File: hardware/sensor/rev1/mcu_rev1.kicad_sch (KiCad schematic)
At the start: 20 parts, among them IC1 STM8L051F3P6, J1 G8250041000YEU, J2 M20-9770342

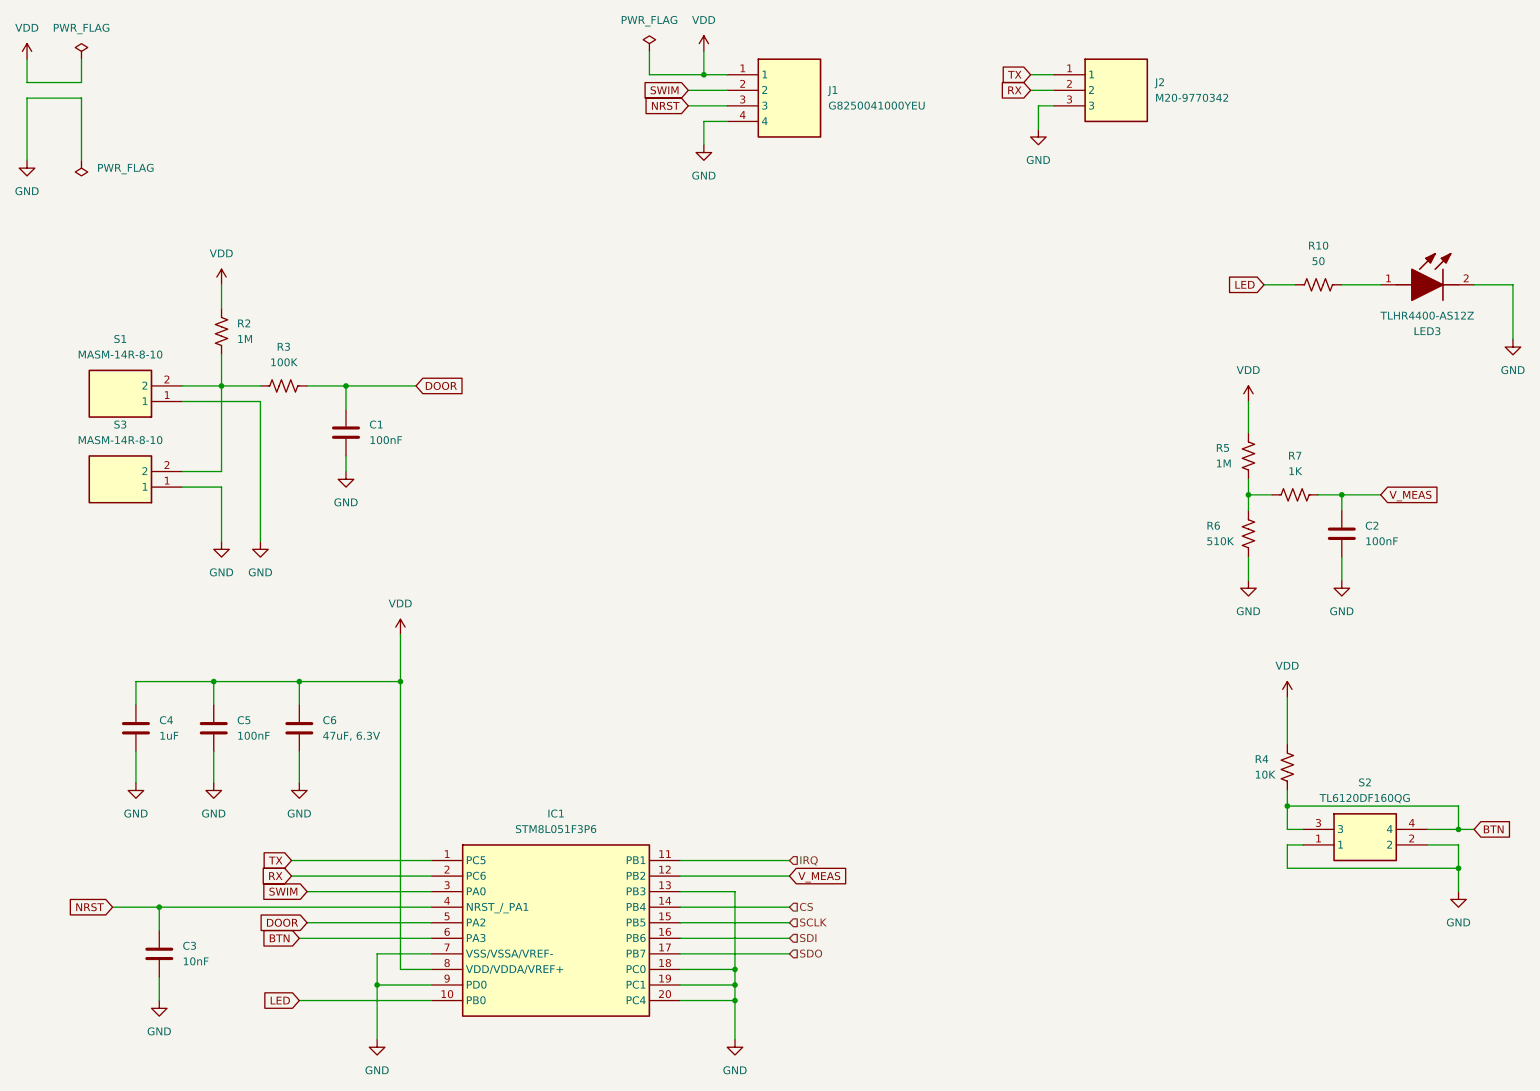
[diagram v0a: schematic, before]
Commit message: EG-49 Several components addes, such as bulk capacitors, battery holder, MCU and reed switches.
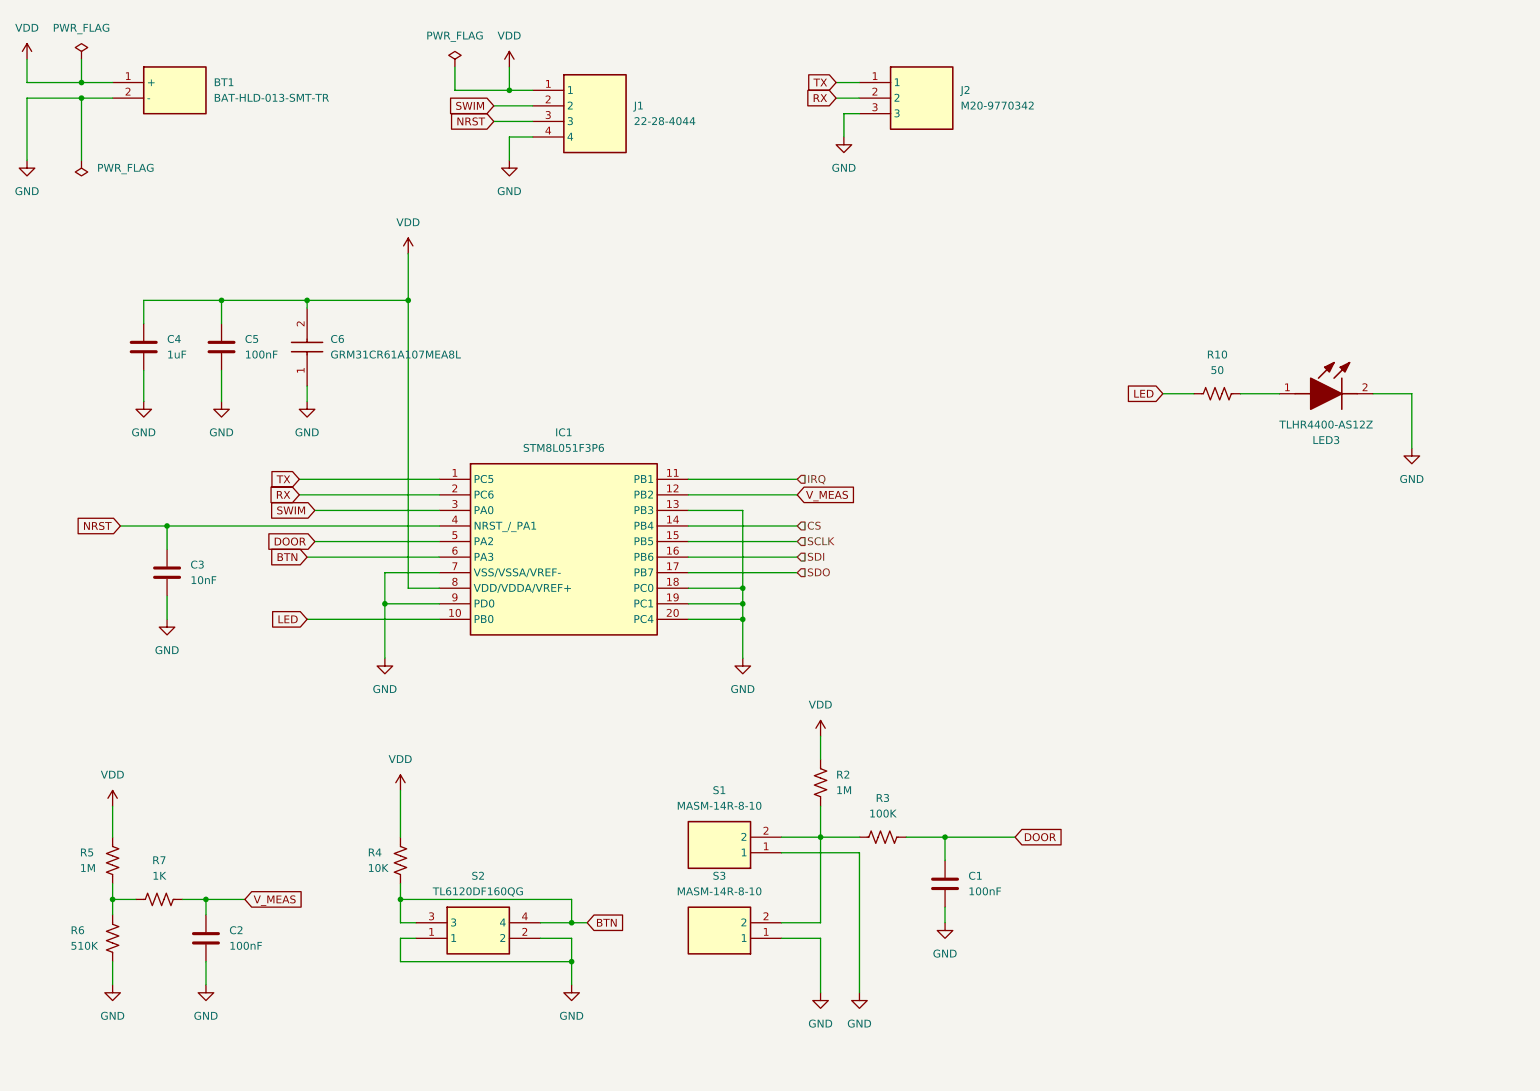
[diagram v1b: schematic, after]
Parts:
- removed C6: 47uF, 6.3V, Capacitor_SMD:C_1206_3216Metric, symbol Device:C
- removed J1: G8250041000YEU, MyParts:HDRV4W55P0X200_1X4_800X200X635P, symbol G8250041000YEU:G8250041000YEU
- added BT1: BAT-HLD-013-SMT-TR, MyParts:BATHLD013SMTTR, symbol BAT-HLD-013-SMT-TR:BAT-HLD-013-SMT-TR
- added C6: GRM31CR61A107MEA8L, MyParts:GRM31x, symbol GRM31CR61A107MEA8L:GRM31CR61A107MEA8L
- added J1: 22-28-4044, MyParts:HDRV4W66P0X254_1X4_1016X249X1067P, symbol 22-28-4044:22-28-4044
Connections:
- net GND: now also BT1.2 (-), C6.1, J1.4
- net NRST: now also J1.3
- net SWIM: now also J1.2
- net VDD: now also BT1.1 (+), C6.2, J1.1
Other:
- moved on the sheet: C1, C2, C3, C4, C5, IC1, J2, LED3, R10, R2, R3, R4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
